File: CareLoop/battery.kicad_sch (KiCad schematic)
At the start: 12 parts, among them J1 Conn_01x02_Pin, J2 USB_B_Micro, J3 Conn_01x02_Pin, U4 MCP1700x-330xxMB, U5 TP4056-42-ESOP8

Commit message: updated version
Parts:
- removed J3: Conn_01x02_Pin, Connector_PinHeader_1.00mm:PinHeader_1x02_P1.00mm_Vertical, symbol Connector:Conn_01x02_Pin
- added C25: 1u, Capacitor_SMD:C_0603_1608Metric_Pad1.08x0.95mm_HandSolder, symbol Device:C_Small
- added C26: 10u, Capacitor_SMD:C_0603_1608Metric_Pad1.08x0.95mm_HandSolder, symbol Device:C_Small
- added JP2_MPU1: Jumper_2_Bridged, Connector_PinHeader_1.00mm:PinHeader_1x02_P1.00mm_Vertical, symbol Jumper:Jumper_2_Bridged
- renumbered J1 to J1_Battery1
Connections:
- net GND: now also J1_Battery1.1 (Pin_1), C25.2, C26.2; no longer U5.8 (CE)
- net at J2.1 (VBUS), R2.2, R6.2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: now also U5.8 (CE), C25.1
- net at J1_Battery1.2 (Pin_2), U5.5 (BAT): now also C26.1, JP2_MPU1.2 (B)
- net at C1.2, C2.2, U4.1 (GND): no longer J1_Battery1.1 (Pin_1)
- net at C2.1, U4.2 (VI): now also JP2_MPU1.1 (A)
- net Dplus: now reaches J2.2 (D-)
- net Dminus: now reaches J2.3 (D+)
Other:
- moved on the sheet: J1_Battery1, R1

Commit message: WP: update Schematics
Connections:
- net VBUS: now reaches C25.1, J2.1 (VBUS), R2.2, R6.2, U5.4 (V_{CC}), U5.8 (CE)
- net Vout renamed VCC
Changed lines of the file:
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@@
+	)
+	(junction
+		(at 121.92 60.96)
+		(diameter 0)
+		(color 0 0 0 0)
 	)
 	(junction
@@
 	(wire
 		(pts
+			(xy 121.92 60.96) (xy 124.46 60.96)
+		)
+		(stroke
+			(width 0)
+			(type default)
+		)
+	)
+	(wire
+		(pts
 			(xy 120.65 91.44) (xy 125.73 91.44)
 		)
@@
 		)
 	)
-	(hierarchical_label "Vout"
+	(hierarchical_label "VCC"
 		(shape output)
 		(at 179.07 80.01 0)
@@
 		(effects
 			(font
+				(size 1.27 1.27)
+			)
+			(justify left)
+		)
+	)
+	(hierarchical_label "VBUS"
+		(shape output)
+		(at 124.46 60.96 0)
+		(effects
+			(font

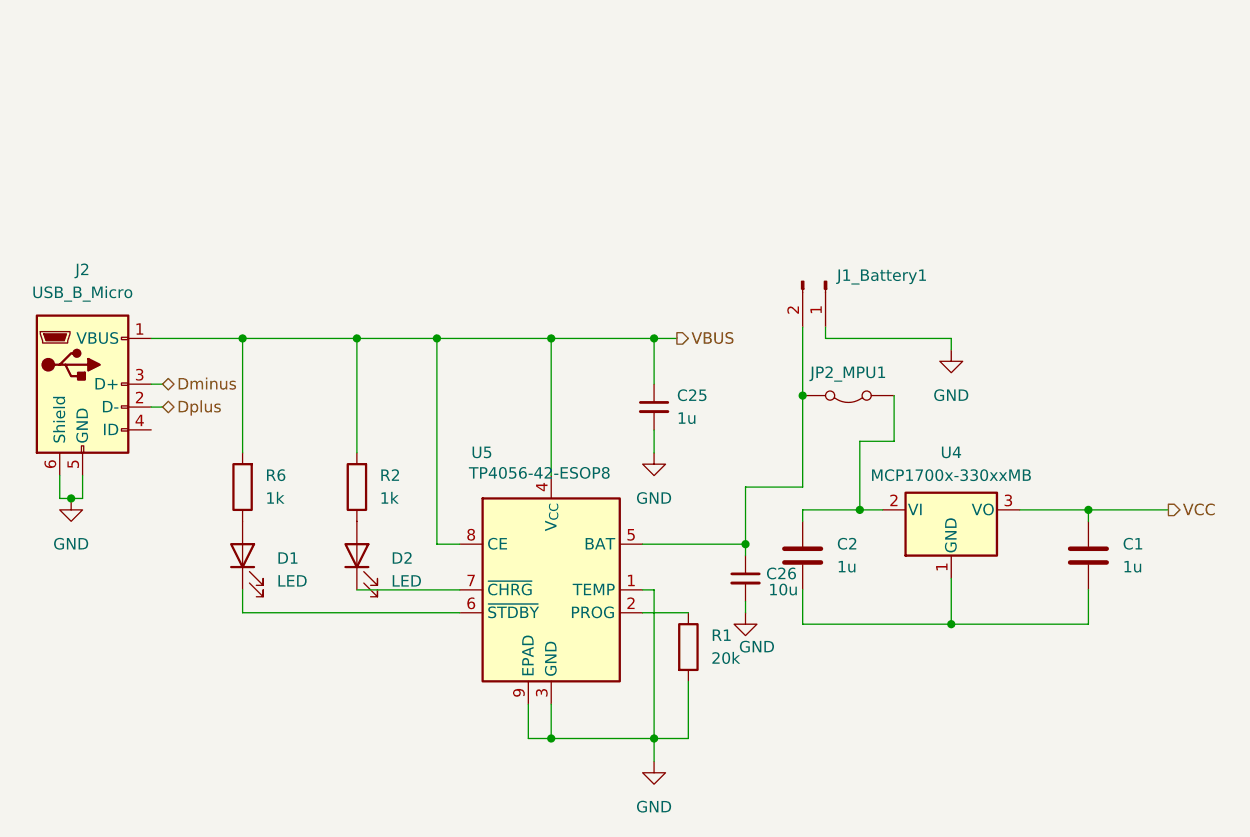
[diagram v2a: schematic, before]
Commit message: WP: Placement PCB Parts done
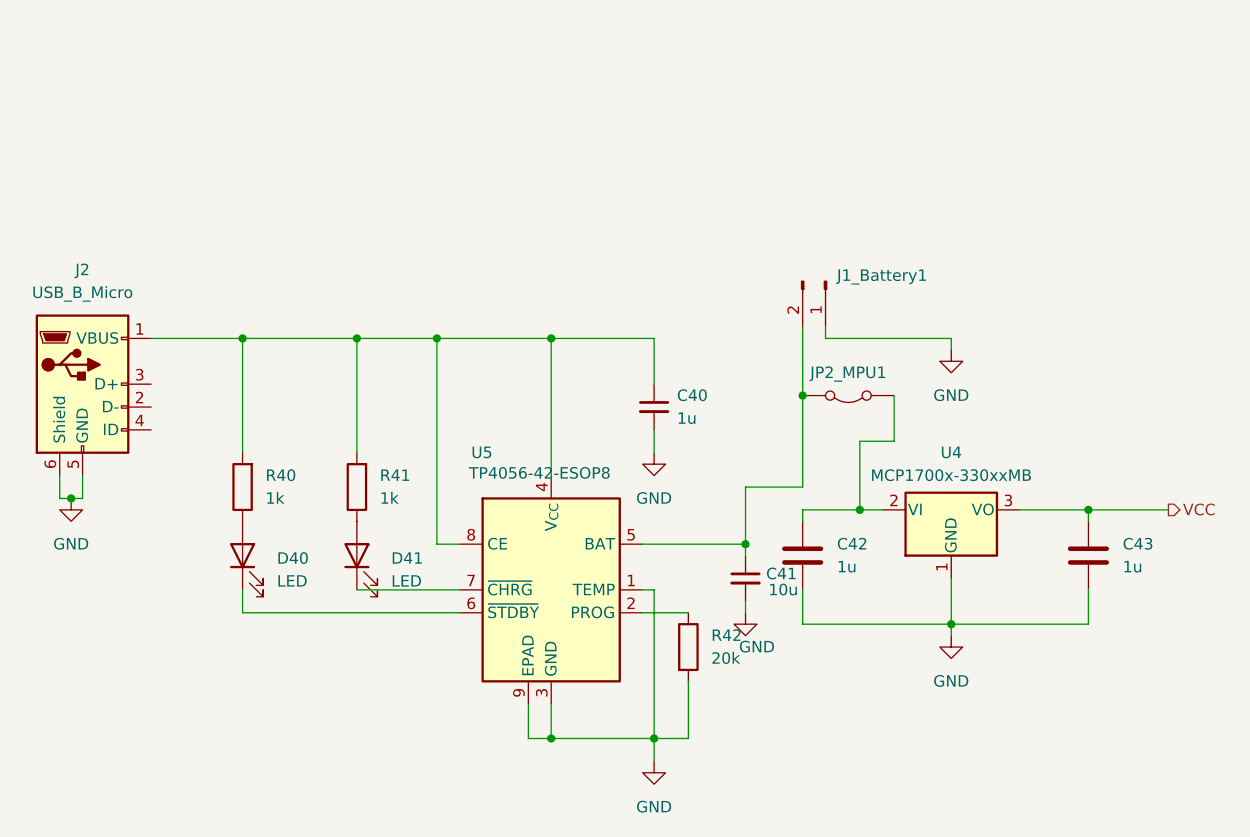
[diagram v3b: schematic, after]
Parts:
- C40: renamed from C25; footprint Capacitor_SMD:C_0603_1608Metric_Pad1.08x0.95mm_HandSolder -> Capacitor_SMD:C_0402_1005Metric_Pad0.74x0.62mm_HandSolder
- C41: renamed from C26; footprint Capacitor_SMD:C_0603_1608Metric_Pad1.08x0.95mm_HandSolder -> Capacitor_SMD:C_0402_1005Metric_Pad0.74x0.62mm_HandSolder
- C42: renamed from C2; footprint Capacitor_SMD:C_0603_1608Metric_Pad1.08x0.95mm_HandSolder -> Capacitor_SMD:C_0402_1005Metric_Pad0.74x0.62mm_HandSolder
- C43: renamed from C1; footprint Capacitor_SMD:C_0603_1608Metric_Pad1.08x0.95mm_HandSolder -> Capacitor_SMD:C_0402_1005Metric_Pad0.74x0.62mm_HandSolder
- D40: renamed from D1; footprint LED_SMD:LED_1206_3216Metric_Pad1.42x1.75mm_HandSolder -> LED_SMD:LED_0402_1005Metric_Pad0.77x0.64mm_HandSolder
- D41: renamed from D2; footprint LED_SMD:LED_1206_3216Metric_Pad1.42x1.75mm_HandSolder -> LED_SMD:LED_0402_1005Metric_Pad0.77x0.64mm_HandSolder
- R40: renamed from R6; footprint Resistor_SMD:R_0603_1608Metric_Pad0.98x0.95mm_HandSolder -> Resistor_SMD:R_0402_1005Metric_Pad0.72x0.64mm_HandSolder
- R41: renamed from R2; footprint Resistor_SMD:R_0603_1608Metric_Pad0.98x0.95mm_HandSolder -> Resistor_SMD:R_0402_1005Metric_Pad0.72x0.64mm_HandSolder
- R42: renamed from R1; footprint Resistor_SMD:R_0603_1608Metric_Pad0.98x0.95mm_HandSolder -> Resistor_SMD:R_0402_1005Metric_Pad0.72x0.64mm_HandSolder
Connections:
- net GND: now also C42.2, C43.2, U4.1 (GND)
- net Dminus: no longer names the net of J2.3 (D+)
- net Dplus: no longer names the net of J2.2 (D-)
- net VBUS: no longer names the net of C40.1, J2.1 (VBUS), R40.2, R41.2, U5.4 (V_{CC}), U5.8 (CE)
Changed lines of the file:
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@@
-	)
-	(junction
-		(at 121.92 60.96)
-		(diameter 0)
-		(color 0 0 0 0)
 	)
 	(junction
@@
 	(wire
 		(pts
-			(xy 66.04 68.58) (xy 67.31 68.58)
-		)
-		(stroke
-			(width 0)
-			(type default)
-		)
-	)
-	(wire
-		(pts
 			(xy 97.79 60.96) (xy 110.49 60.96)
 		)
@@
 	(wire
 		(pts
-			(xy 66.04 66.04) (xy 67.31 66.04)
-		)
-		(stroke
-			(width 0)
-			(type default)
-		)
-	)
-	(wire
-		(pts
 			(xy 132.08 90.17) (xy 132.08 91.44)
 		)
@@
 	(wire
 		(pts
+			(xy 154.94 92.71) (xy 154.94 93.98)
+		)
+		(stroke
+			(width 0)
+			(type default)
+		)
+	)
+	(wire
+		(pts
 			(xy 154.94 92.71) (xy 170.18 92.71)
-		)
-		(stroke
-			(width 0)
-			(type default)
-		)
-	)
-	(wire
-		(pts
-			(xy 121.92 60.96) (xy 124.46 60.96)
 		)
 		(stroke
@@
 		)
 	)
-	(hierarchical_label "Dplus"
-		(shape bidirectional)
-		(at 67.31 68.58 0)
-		(effects
-			(font
-				(size 1.27 1.27)
-			)
-			(justify left)
-		)
-	)
-	(hierarchical_label "VBUS"
-		(shape output)
-		(at 124.46 60.96 0)
-		(effects
-			(font
-				(size 1.27 1.27)
-			)
-			(justify left)
-		)
-	)
-	(hierarchical_label "Dminus"
-		(shape bidirectional)
-		(at 67.31 66.04 0)
-		(effects
-			(font
-				(size 1.27 1.27)
-			)
-			(justify left)
-		)
-	)
 	(symbol
 		(lib_id "Device:R")
@@
 		(dnp no)
 		(fields_autoplaced yes)
-		(property "Reference" "R6"
+		(property "Reference" "R40"
 			(at 78.74 76.1999 0)
 			(effects
@@
 			)
 		)
-		(property "Footprint" "Resistor_SMD:R_0603_1608Metric_Pad0.98x0.95mm_HandSolder"
+		(property "Footprint" "Resistor_SMD:R_0402_1005Metric_Pad0.72x0.64mm_HandSolder"
 			(at 77.978 77.47 90)
 			(effects
@@
 			(project ""
 				(path "/1249f778-de2d-49b4-b768-08b76b87278f/229629cb-a49c-4768-b0e8-d6cfdb6777f2"
-					(reference "R6")
+					(reference "R40")
 					(unit 1)
 				)
@@
 		(on_board yes)
 		(dnp no)
-		(property "Reference" "C26"
+		(property "Reference" "C41"
 			(at 134.366 87.122 0)
 			(effects
@@
 			)
 		)
-		(property "Footprint" "Capacitor_SMD:C_0603_1608Metric_Pad1.08x0.95mm_HandSolder"
+		(property "Footprint" "Capacitor_SMD:C_0402_1005Metric_Pad0.74x0.62mm_HandSolder"
 			(at 132.08 87.63 0)
 			(effects
@@
 			(project "CareLoop_PCB"
 				(path "/1249f778-de2d-49b4-b768-08b76b87278f/229629cb-a49c-4768-b0e8-d6cfdb6777f2"
-					(reference "C26")
+					(reference "C41")
 					(unit 1)
 				)
@@
 	)
 	(symbol
+		(lib_id "power:GND")
+		(at 154.94 93.98 0)
+		(unit 1)
+		(exclude_from_sim no)
+		(in_bom yes)
+		(on_board yes)
+		(dnp no)
+		(fields_autoplaced yes)
+		(property "Reference" "#PWR029"
+			(at 154.94 100.33 0)
+			(effects
+				(font
+					(size 1.27 1.27)
+				)
+				(hide yes)
+			)
+		)
+		(property "Value" "GND"
+			(at 154.94 99.06 0)
+			(effects
+				(font
+					(size 1.27 1.27)
+				)
+			)
+		)
+		(property "Footprint" ""
+			(at 154.94 93.98 0)
+			(effects
+				(font
+					(size 1.27 1.27)
+				)
+				(hide yes)
+			)
+		)
+		(property "Datasheet" ""
+			(at 154.94 93.98 0)
+			(effects
+				(font
+					(size 1.27 1.27)
+				)
+				(hide yes)
+			)
+		)
+		(property "Description" "Power symbol creates a global label with name \"GND\" , ground"
+			(at 154.94 93.98 0)
+			(effects
+				(font
+					(size 1.27 1.27)
+				)
+				(hide yes)
+			)
+		)
+		(pin "1"
+		)
+		(instances
+			(project ""
+				(path "/1249f778-de2d-49b4-b768-08b76b87278f/229629cb-a49c-4768-b0e8-d6cfdb6777f2"
+					(reference "#PWR029")
+					(unit 1)
+				)
+			)
+		)
+	)
+	(symbol
 		(lib_id "Jumper:Jumper_2_Bridged")
 		(at 143.51 67.31 180)
@@
 		(dnp no)
 		(fields_autoplaced yes)
-		(property "Reference" "C1"
+		(property "Reference" "C43"
 			(at 173.99 83.8199 0)
 			(effects
@@
 			)
 		)
-		(property "Footprint" "Capacitor_SMD:C_0603_1608Metric_Pad1.08x0.95mm_HandSolder"
+		(property "Footprint" "Capacitor_SMD:C_0402_1005Metric_Pad0.74x0.62mm_HandSolder"
 			(at 171.1452 88.9 0)
 			(effects
@@
 			(project ""
 				(path "/1249f778-de2d-49b4-b768-08b76b87278f/229629cb-a49c-4768-b0e8-d6cfdb6777f2"
-					(reference "C1")
+					(reference "C43")
 					(unit 1)
 				)
@@
 		(dnp no)
 		(fields_autoplaced yes)
-		(property "Reference" "C2"
+		(property "Reference" "C42"
 			(at 142.24 83.8199 0)
 			(effects
@@
 			)
 		)
-		(property "Footprint" "Capacitor_SMD:C_0603_1608Metric_Pad1.08x0.95mm_HandSolder"
+		(property "Footprint" "Capacitor_SMD:C_0402_1005Metric_Pad0.74x0.62mm_HandSolder"
 			(at 139.3952 88.9 0)
 			(effects
@@
 			(project ""
 				(path "/1249f778-de2d-49b4-b768-08b76b87278f/229629cb-a49c-4768-b0e8-d6cfdb6777f2"
-					(reference "C2")
+					(reference "C42")
 					(unit 1)
 				)
@@
 		(dnp no)
 		(fields_autoplaced yes)
-		(property "Reference" "D2"
+		(property "Reference" "D41"
 			(at 92.71 85.4074 90)
 			(effects
@@
 			)
 		)
-		(property "Footprint" "LED_SMD:LED_1206_3216Metric_Pad1.42x1.75mm_HandSolder"
+		(property "Footprint" "LED_SMD:LED_0402_1005Metric_Pad0.77x0.64mm_HandSolder"
 			(at 88.9 85.09 0)
 			(effects
@@
 			(project ""
 				(path "/1249f778-de2d-49b4-b768-08b76b87278f/229629cb-a49c-4768-b0e8-d6cfdb6777f2"
-					(reference "D2")
+					(reference "D41")
 					(unit 1)
 				)
@@
 		(dnp no)
 		(fields_autoplaced yes)
-		(property "Reference" "C25"
+		(property "Reference" "C40"
 			(at 124.46 67.3162 0)
 			(effects
@@
 			)
 		)
-		(property "Footprint" "Capacitor_SMD:C_0603_1608Metric_Pad1.08x0.95mm_HandSolder"
+		(property "Footprint" "Capacitor_SMD:C_0402_1005Metric_Pad0.74x0.62mm_HandSolder"
 			(at 121.92 68.58 0)
 			(effects
@@
 			(project ""
 				(path "/1249f778-de2d-49b4-b768-08b76b87278f/229629cb-a49c-4768-b0e8-d6cfdb6777f2"
-					(reference "C25")
+					(reference "C40")
 					(unit 1)
 				)
@@
 		(dnp no)
 		(fields_autoplaced yes)
-		(property "Reference" "D1"
+		(property "Reference" "D40"
 			(at 80.01 85.4074 90)
 			(effects
@@
 			)
 		)
-		(property "Footprint" "LED_SMD:LED_1206_3216Metric_Pad1.42x1.75mm_HandSolder"
+		(property "Footprint" "LED_SMD:LED_0402_1005Metric_Pad0.77x0.64mm_HandSolder"
 			(at 76.2 85.09 0)
 			(effects
@@
 			(project ""
 				(path "/1249f778-de2d-49b4-b768-08b76b87278f/229629cb-a49c-4768-b0e8-d6cfdb6777f2"
-					(reference "D1")
+					(reference "D40")
 					(unit 1)
 				)
@@
 		(dnp no)
 		(fields_autoplaced yes)
-		(property "Reference" "R2"
+		(property "Reference" "R41"
 			(at 91.44 76.1999 0)
 			(effects
@@
 			)
 		)
-		(property "Footprint" "Resistor_SMD:R_0603_1608Metric_Pad0.98x0.95mm_HandSolder"
+		(property "Footprint" "Resistor_SMD:R_0402_1005Metric_Pad0.72x0.64mm_HandSolder"
 			(at 90.678 77.47 90)
 			(effects
@@
 			(project ""
 				(path "/1249f778-de2d-49b4-b768-08b76b87278f/229629cb-a49c-4768-b0e8-d6cfdb6777f2"
-					(reference "R2")
+					(reference "R41")
 					(unit 1)
 				)
@@
 		(dnp no)
 		(fields_autoplaced yes)
-		(property "Reference" "R1"
+		(property "Reference" "R42"
 			(at 128.27 93.9799 0)
 			(effects
@@
 			)
 		)
-		(property "Footprint" "Resistor_SMD:R_0603_1608Metric_Pad0.98x0.95mm_HandSolder"
+		(property "Footprint" "Resistor_SMD:R_0402_1005Metric_Pad0.72x0.64mm_HandSolder"
 			(at 123.952 95.25 90)
 			(effects
@@
 			(project ""
 				(path "/1249f778-de2d-49b4-b768-08b76b87278f/229629cb-a49c-4768-b0e8-d6cfdb6777f2"
-					(reference "R1")
-					(unit 1)
-				)
+					(reference "R42")
+					(unit 1)
+				)

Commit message: update routing
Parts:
- U5: footprint Package_SO:SOIC-8-1EP_3.9x4.9mm_P1.27mm_EP2.41x3.3mm_ThermalVias -> Package_SO:SOIC-8-1EP_3.9x4.9mm_P1.27mm_EP2.41x3.81mm
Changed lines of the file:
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@@
 			)
 		)
-		(property "Footprint" "Package_SO:SOIC-8-1EP_3.9x4.9mm_P1.27mm_EP2.41x3.3mm_ThermalVias"
+		(property "Footprint" "Package_SO:SOIC-8-1EP_3.9x4.9mm_P1.27mm_EP2.41x3.81mm"
 			(at 110.998 111.76 0)
 			(effects

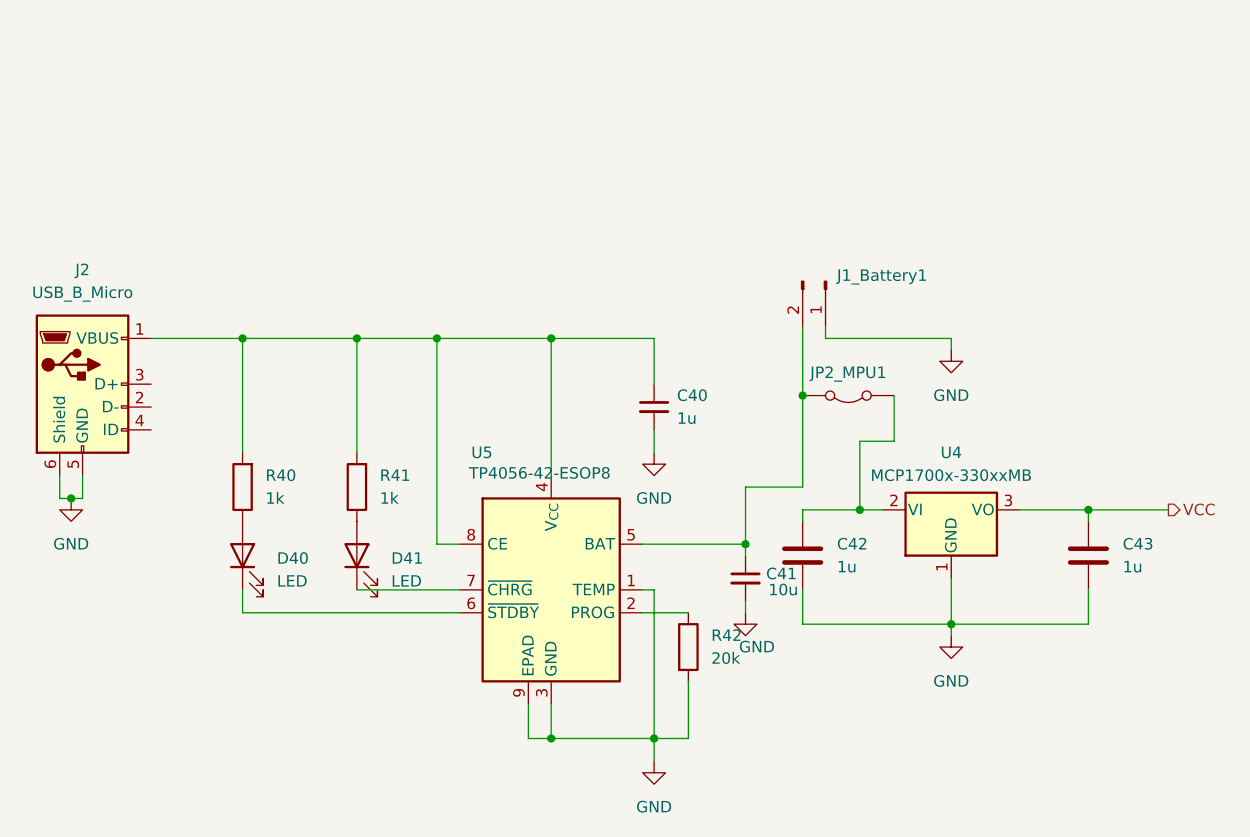
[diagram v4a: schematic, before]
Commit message: updated vias
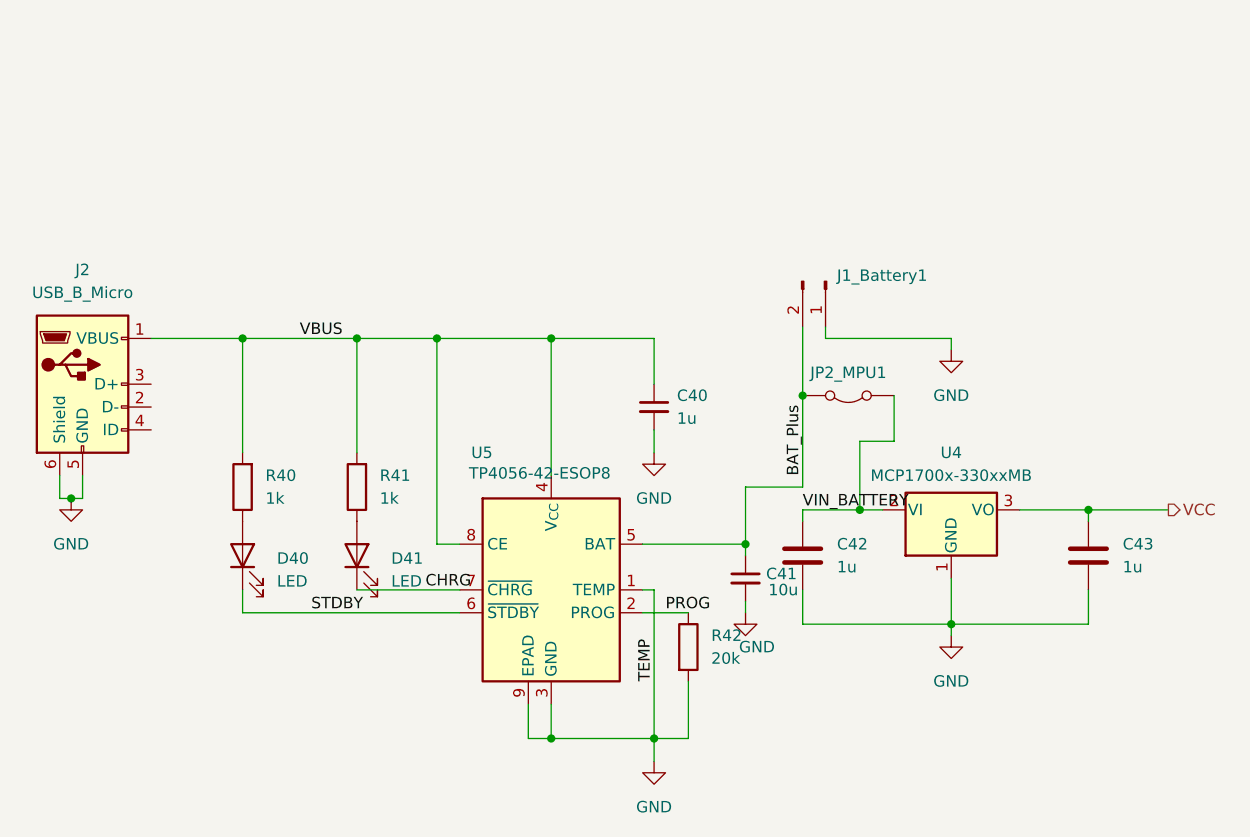
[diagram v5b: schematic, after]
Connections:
- net VBUS: now reaches C40.1, J2.1 (VBUS), R40.2, R41.2, U5.4 (V_{CC}), U5.8 (CE)
- net BAT_Plus: now reaches C41.1, J1_Battery1.2 (Pin_2), JP2_MPU1.2 (B), U5.5 (BAT)
- net VIN_BATTERY: now reaches C42.1, JP2_MPU1.1 (A), U4.2 (VI)
- net PROG: now reaches R42.1, U5.2 (PROG)
- net STDBY: now reaches D40.1 (K), U5.6 (~{STDBY})
- net CHRG: now reaches D41.1 (K), U5.7 (~{CHRG})
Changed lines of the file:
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@@
+		)
+	)
+	(label "VBUS"
+		(at 82.55 60.96 0)
+		(effects
+			(font
+				(size 1.27 1.27)
+			)
+			(justify left bottom)
+		)
+	)
+	(label "BAT_Plus"
+		(at 138.43 76.2 90)
+		(effects
+			(font
+				(size 1.27 1.27)
+			)
+			(justify left bottom)
+		)
+	)
+	(label "VIN_BATTERY"
+		(at 138.43 80.01 0)
+		(effects
+			(font
+				(size 1.27 1.27)
+			)
+			(justify left bottom)
+		)
+	)
+	(label "TEMP"
+		(at 121.92 99.06 90)
+		(effects
+			(font
+				(size 1.27 1.27)
+			)
+			(justify left bottom)
+		)
+	)
+	(label "CHRG"
+		(at 96.52 88.9 0)
+		(effects
+			(font
+				(size 1.27 1.27)
+			)
+			(justify left bottom)
+		)
+	)
+	(label "STDBY"
+		(at 83.82 91.44 0)
+		(effects
+			(font
+				(size 1.27 1.27)
+			)
+			(justify left bottom)
+		)
+	)
+	(label "PROG"
+		(at 123.19 91.44 0)
+		(effects
+			(font
+				(size 1.27 1.27)
+			)
+			(justify left bottom)
 		)
 	)

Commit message: PCB update
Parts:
- U4: footprint Package_TO_SOT_SMD:SOT-89-3 -> Package_TO_SOT_SMD:SOT-23
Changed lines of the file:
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@@
 			)
 		)
-		(property "Footprint" "Package_TO_SOT_SMD:SOT-89-3"
+		(property "Footprint" "Package_TO_SOT_SMD:SOT-23"
 			(at 154.94 74.93 0)
 			(effects
